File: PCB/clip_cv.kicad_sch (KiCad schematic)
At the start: 5 parts, among them J4 Input

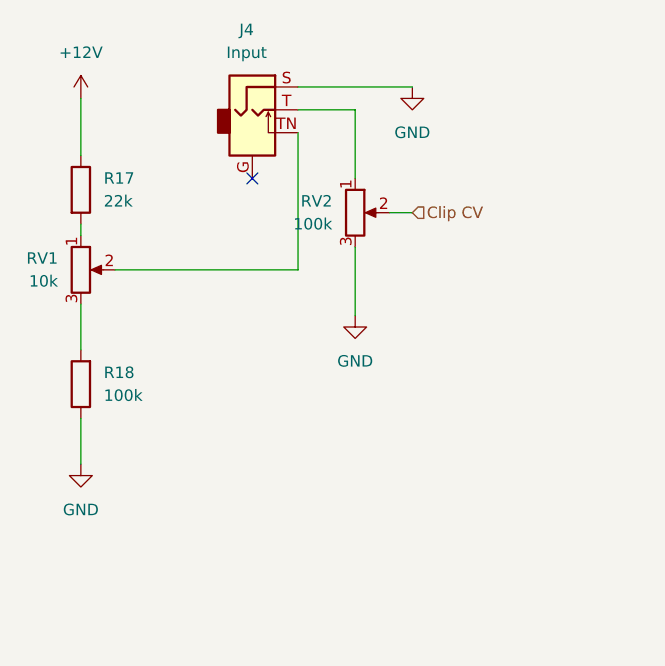
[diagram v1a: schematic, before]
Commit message: :art: Adjust layout of Clip CV input
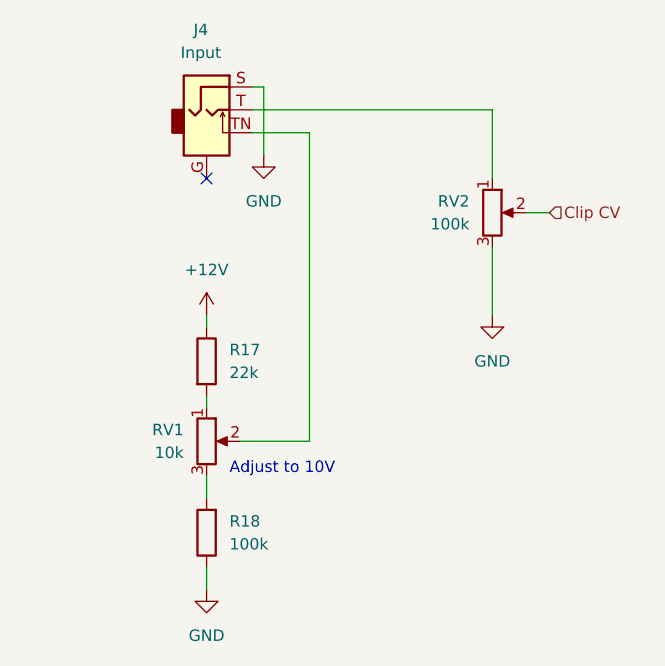
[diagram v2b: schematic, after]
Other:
- note added: "Adjust to 10V"
- moved on the sheet: J4, R17, R18, RV1, RV2

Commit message: :wrench: Re-assign component designators
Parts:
- renumbered R17 to R15, R18 to R16
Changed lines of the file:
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@@
   (symbol (lib_id "power:+12V") (at 149.86 102.87 0) (unit 1)
     (in_bom yes) (on_board yes) (dnp no) (fields_autoplaced)
-    (property "Reference" "#PWR0126" (at 149.86 106.68 0)
+    (property "Reference" "#PWR023" (at 149.86 106.68 0)
       (effects (font (size 1.27 1.27)) hide)
     )
@@
       (project "misterclippy"
         (path "/e63e39d7-6ac0-4ffd-8aa3-1841a4541b55/82b4cd66-2d39-4c64-8856-8f0d15c030b3"
-          (reference "#PWR0126") (unit 1)
-        )
-        (path "/e63e39d7-6ac0-4ffd-8aa3-1841a4541b55/99ffd22e-688e-45fd-ad48-7239527f44b1"
-          (reference "#PWR0130") (unit 1)
+          (reference "#PWR023") (unit 1)
+        )
+        (path "/e63e39d7-6ac0-4ffd-8aa3-1841a4541b55/99ffd22e-688e-45fd-ad48-7239527f44b1"
+          (reference "#PWR027") (unit 1)
         )
       )
@@
   (symbol (lib_id "Device:R") (at 149.86 107.95 0) (unit 1)
     (in_bom yes) (on_board yes) (dnp no) (fields_autoplaced)
-    (property "Reference" "R17" (at 152.4 106.6799 0)
+    (property "Reference" "R15" (at 152.4 106.6799 0)
       (effects (font (size 1.27 1.27)) (justify left))
     )
@@
       (project "misterclippy"
         (path "/e63e39d7-6ac0-4ffd-8aa3-1841a4541b55/82b4cd66-2d39-4c64-8856-8f0d15c030b3"
+          (reference "R15") (unit 1)
+        )
+        (path "/e63e39d7-6ac0-4ffd-8aa3-1841a4541b55/99ffd22e-688e-45fd-ad48-7239527f44b1"
           (reference "R17") (unit 1)
         )
-        (path "/e63e39d7-6ac0-4ffd-8aa3-1841a4541b55/99ffd22e-688e-45fd-ad48-7239527f44b1"
-          (reference "R19") (unit 1)
-        )
       )
     )
@@
   (symbol (lib_id "power:GND") (at 156.21 85.09 0) (unit 1)
     (in_bom yes) (on_board yes) (dnp no) (fields_autoplaced)
-    (property "Reference" "#PWR0127" (at 156.21 91.44 0)
+    (property "Reference" "#PWR025" (at 156.21 91.44 0)
       (effects (font (size 1.27 1.27)) hide)
     )
@@
       (project "misterclippy"
         (path "/e63e39d7-6ac0-4ffd-8aa3-1841a4541b55/82b4cd66-2d39-4c64-8856-8f0d15c030b3"
-          (reference "#PWR0127") (unit 1)
-        )
-        (path "/e63e39d7-6ac0-4ffd-8aa3-1841a4541b55/99ffd22e-688e-45fd-ad48-7239527f44b1"
-          (reference "#PWR0131") (unit 1)
+          (reference "#PWR025") (unit 1)
+        )
+        (path "/e63e39d7-6ac0-4ffd-8aa3-1841a4541b55/99ffd22e-688e-45fd-ad48-7239527f44b1"
+          (reference "#PWR029") (unit 1)
         )
       )
@@
   (symbol (lib_id "power:GND") (at 149.86 133.35 0) (unit 1)
     (in_bom yes) (on_board yes) (dnp no) (fields_autoplaced)
-    (property "Reference" "#PWR0125" (at 149.86 139.7 0)
+    (property "Reference" "#PWR024" (at 149.86 139.7 0)
       (effects (font (size 1.27 1.27)) hide)
     )
@@
       (project "misterclippy"
         (path "/e63e39d7-6ac0-4ffd-8aa3-1841a4541b55/82b4cd66-2d39-4c64-8856-8f0d15c030b3"
-          (reference "#PWR0125") (unit 1)
-        )
-        (path "/e63e39d7-6ac0-4ffd-8aa3-1841a4541b55/99ffd22e-688e-45fd-ad48-7239527f44b1"
-          (reference "#PWR0129") (unit 1)
+          (reference "#PWR024") (unit 1)
+        )
+        (path "/e63e39d7-6ac0-4ffd-8aa3-1841a4541b55/99ffd22e-688e-45fd-ad48-7239527f44b1"
+          (reference "#PWR028") (unit 1)
         )
       )
@@
   (symbol (lib_id "Device:R") (at 149.86 127 180) (unit 1)
     (in_bom yes) (on_board yes) (dnp no) (fields_autoplaced)
-    (property "Reference" "R18" (at 152.4 125.7299 0)
+    (property "Reference" "R16" (at 152.4 125.7299 0)
       (effects (font (size 1.27 1.27)) (justify right))
     )
@@
       (project "misterclippy"
         (path "/e63e39d7-6ac0-4ffd-8aa3-1841a4541b55/82b4cd66-2d39-4c64-8856-8f0d15c030b3"
+          (reference "R16") (unit 1)
+        )
+        (path "/e63e39d7-6ac0-4ffd-8aa3-1841a4541b55/99ffd22e-688e-45fd-ad48-7239527f44b1"
           (reference "R18") (unit 1)
         )
-        (path "/e63e39d7-6ac0-4ffd-8aa3-1841a4541b55/99ffd22e-688e-45fd-ad48-7239527f44b1"
-          (reference "R20") (unit 1)
-        )
       )
     )
@@
   (symbol (lib_id "power:GND") (at 181.61 102.87 0) (unit 1)
     (in_bom yes) (on_board yes) (dnp no) (fields_autoplaced)
-    (property "Reference" "#PWR0128" (at 181.61 109.22 0)
+    (property "Reference" "#PWR026" (at 181.61 109.22 0)
       (effects (font (size 1.27 1.27)) hide)
     )
@@
       (project "misterclippy"
         (path "/e63e39d7-6ac0-4ffd-8aa3-1841a4541b55/82b4cd66-2d39-4c64-8856-8f0d15c030b3"
-          (reference "#PWR0128") (unit 1)
-        )
-        (path "/e63e39d7-6ac0-4ffd-8aa3-1841a4541b55/99ffd22e-688e-45fd-ad48-7239527f44b1"
-          (reference "#PWR0132") (unit 1)
-        )
-      )
+          (reference "#PWR026") (unit 1)
+        )
+        (path "/e63e39d7-6ac0-4ffd-8aa3-1841a4541b55/99ffd22e-688e-45fd-ad48-7239527f44b1"
+          (reference "#PWR030") (unit 1)
+        )
+      )

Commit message: :wrench: Replace audio jack footprints by centered versions
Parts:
- J4: footprint Connector_Audio:Jack_3.5mm_QingPu_WQP-PJ398SM_Vertical_CircularHoles -> mopsy:Jack_3.5mm_QingPu_WQP-PJ398SM_Vertical_CircularHoles_Centered
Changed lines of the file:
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@@
       (effects (font (size 1.27 1.27)))
     )
-    (property "Footprint" "Connector_Audio:Jack_3.5mm_QingPu_WQP-PJ398SM_Vertical_CircularHoles" (at 149.86 80.01 0)
+    (property "Footprint" "mopsy:Jack_3.5mm_QingPu_WQP-PJ398SM_Vertical_CircularHoles_Centered" (at 149.86 80.01 0)
       (effects (font (size 1.27 1.27)) hide)
     )

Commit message: :art: Turn poti direction around
Make sure that turning the poti clockwise increases the setting.
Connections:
- net GND: now also RV2.1; no longer RV2.3
- net at R15.2: now also RV1.3; no longer RV1.1
- net at R16.2: now also RV1.1; no longer RV1.3
- net at J4.T: now also RV2.3; no longer RV2.1
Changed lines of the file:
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@@
     )
   )
-  (symbol (lib_id "Device:R_Potentiometer") (at 149.86 116.84 0) (unit 1)
-    (in_bom yes) (on_board yes) (dnp no) (fields_autoplaced)
-    (property "Reference" "RV1" (at 147.32 115.5699 0)
+  (symbol (lib_id "Device:R_Potentiometer") (at 149.86 116.84 0) (mirror x) (unit 1)
+    (in_bom yes) (on_board yes) (dnp no)
+    (property "Reference" "RV1" (at 147.32 118.1101 0)
       (effects (font (size 1.27 1.27)) (justify right))
     )
-    (property "Value" "10k" (at 147.32 118.1099 0)
+    (property "Value" "10k" (at 147.32 115.5701 0)
       (effects (font (size 1.27 1.27)) (justify right))
     )
@@
     )
   )
-  (symbol (lib_id "Device:R_Potentiometer") (at 181.61 91.44 0) (unit 1)
-    (in_bom yes) (on_board yes) (dnp no) (fields_autoplaced)
-    (property "Reference" "RV2" (at 179.07 90.1699 0)
+  (symbol (lib_id "Device:R_Potentiometer") (at 181.61 91.44 0) (mirror x) (unit 1)
+    (in_bom yes) (on_board yes) (dnp no)
+    (property "Reference" "RV2" (at 179.07 92.7101 0)
       (effects (font (size 1.27 1.27)) (justify right))
     )
-    (property "Value" "100k" (at 179.07 92.7099 0)
+    (property "Value" "100k" (at 179.07 90.1701 0)
       (effects (font (size 1.27 1.27)) (justify right))
     )

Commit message: :art: Apply geographical reannotation
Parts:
- renumbered J4 to J5, R16 to R15, R15 to R16, RV2 to RV1, RV1 to RV4
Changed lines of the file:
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@@
   (symbol (lib_id "Device:R") (at 149.86 107.95 0) (unit 1)
     (in_bom yes) (on_board yes) (dnp no) (fields_autoplaced)
-    (property "Reference" "R15" (at 152.4 106.6799 0)
+    (property "Reference" "R16" (at 152.4 106.6799 0)
       (effects (font (size 1.27 1.27)) (justify left))
     )
@@
       (project "misterclippy"
         (path "/e63e39d7-6ac0-4ffd-8aa3-1841a4541b55/82b4cd66-2d39-4c64-8856-8f0d15c030b3"
-          (reference "R15") (unit 1)
+          (reference "R16") (unit 1)
         )
         (path "/e63e39d7-6ac0-4ffd-8aa3-1841a4541b55/99ffd22e-688e-45fd-ad48-7239527f44b1"
-          (reference "R17") (unit 1)
+          (reference "R14") (unit 1)
         )
       )
@@
   (symbol (lib_id "Device:R_Potentiometer") (at 149.86 116.84 0) (mirror x) (unit 1)
     (in_bom yes) (on_board yes) (dnp no)
-    (property "Reference" "RV1" (at 147.32 118.1101 0)
+    (property "Reference" "RV4" (at 147.32 118.1101 0)
       (effects (font (size 1.27 1.27)) (justify right))
     )
@@
       (project "misterclippy"
         (path "/e63e39d7-6ac0-4ffd-8aa3-1841a4541b55/82b4cd66-2d39-4c64-8856-8f0d15c030b3"
-          (reference "RV1") (unit 1)
+          (reference "RV4") (unit 1)
         )
         (path "/e63e39d7-6ac0-4ffd-8aa3-1841a4541b55/99ffd22e-688e-45fd-ad48-7239527f44b1"
@@
   (symbol (lib_id "Device:R_Potentiometer") (at 181.61 91.44 0) (mirror x) (unit 1)
     (in_bom yes) (on_board yes) (dnp no)
-    (property "Reference" "RV2" (at 179.07 92.7101 0)
+    (property "Reference" "RV1" (at 179.07 92.7101 0)
       (effects (font (size 1.27 1.27)) (justify right))
     )
@@
       (project "misterclippy"
         (path "/e63e39d7-6ac0-4ffd-8aa3-1841a4541b55/82b4cd66-2d39-4c64-8856-8f0d15c030b3"
-          (reference "RV2") (unit 1)
+          (reference "RV1") (unit 1)
         )
         (path "/e63e39d7-6ac0-4ffd-8aa3-1841a4541b55/99ffd22e-688e-45fd-ad48-7239527f44b1"
-          (reference "RV4") (unit 1)
+          (reference "RV2") (unit 1)
         )
       )
@@
   (symbol (lib_id "Connector:AudioJack2_Ground_SwitchT") (at 149.86 80.01 0) (unit 1)
     (in_bom yes) (on_board yes) (dnp no) (fields_autoplaced)
-    (property "Reference" "J4" (at 149.225 71.12 0)
+    (property "Reference" "J5" (at 149.225 71.12 0)
       (effects (font (size 1.27 1.27)))
     )
@@
       (project "misterclippy"
         (path "/e63e39d7-6ac0-4ffd-8aa3-1841a4541b55/82b4cd66-2d39-4c64-8856-8f0d15c030b3"
-          (reference "J4") (unit 1)
+          (reference "J5") (unit 1)
         )
         (path "/e63e39d7-6ac0-4ffd-8aa3-1841a4541b55/99ffd22e-688e-45fd-ad48-7239527f44b1"
-          (reference "J5") (unit 1)
+          (reference "J6") (unit 1)
         )
       )
@@
   (symbol (lib_id "Device:R") (at 149.86 127 180) (unit 1)
     (in_bom yes) (on_board yes) (dnp no) (fields_autoplaced)
-    (property "Reference" "R16" (at 152.4 125.7299 0)
+    (property "Reference" "R15" (at 152.4 125.7299 0)
       (effects (font (size 1.27 1.27)) (justify right))
     )
@@
       (project "misterclippy"
         (path "/e63e39d7-6ac0-4ffd-8aa3-1841a4541b55/82b4cd66-2d39-4c64-8856-8f0d15c030b3"
-          (reference "R16") (unit 1)
+          (reference "R15") (unit 1)
         )
         (path "/e63e39d7-6ac0-4ffd-8aa3-1841a4541b55/99ffd22e-688e-45fd-ad48-7239527f44b1"
-          (reference "R18") (unit 1)
+          (reference "R13") (unit 1)
         )
       )

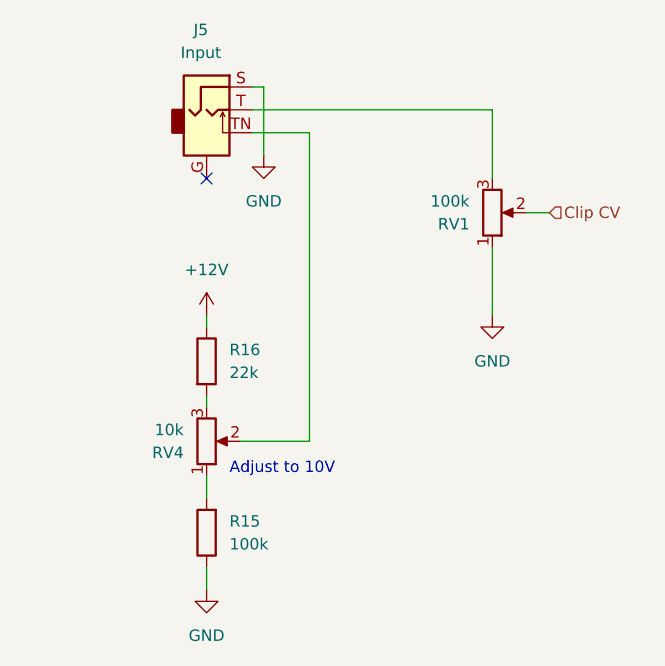
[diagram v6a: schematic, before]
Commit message: :art: Adjust voltage divider for Clip CV tap
Adjust the voltage divider so that 10V are within a good
adjustment range.
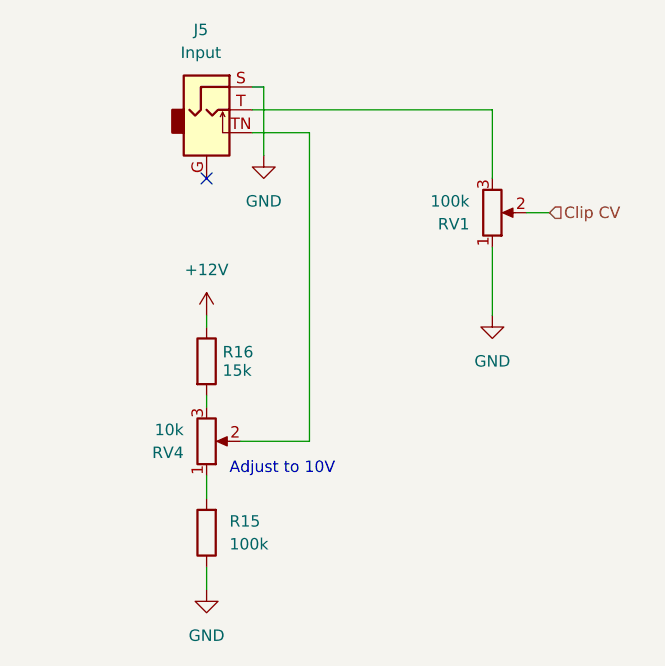
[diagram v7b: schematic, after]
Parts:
- R16: value 22k -> 15k
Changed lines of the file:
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@@
   (symbol (lib_id "Device:R") (at 149.86 107.95 0) (unit 1)
     (in_bom yes) (on_board yes) (dnp no) (fields_autoplaced)
-    (property "Reference" "R16" (at 152.4 106.6799 0)
+    (property "Reference" "R16" (at 151.638 106.926 0)
       (effects (font (size 1.27 1.27)) (justify left))
     )
-    (property "Value" "22k" (at 152.4 109.2199 0)
+    (property "Value" "15k" (at 151.638 108.974 0)
       (effects (font (size 1.27 1.27)) (justify left))
     )

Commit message: :wrench: Adjust the voltage dividers for Clip CV
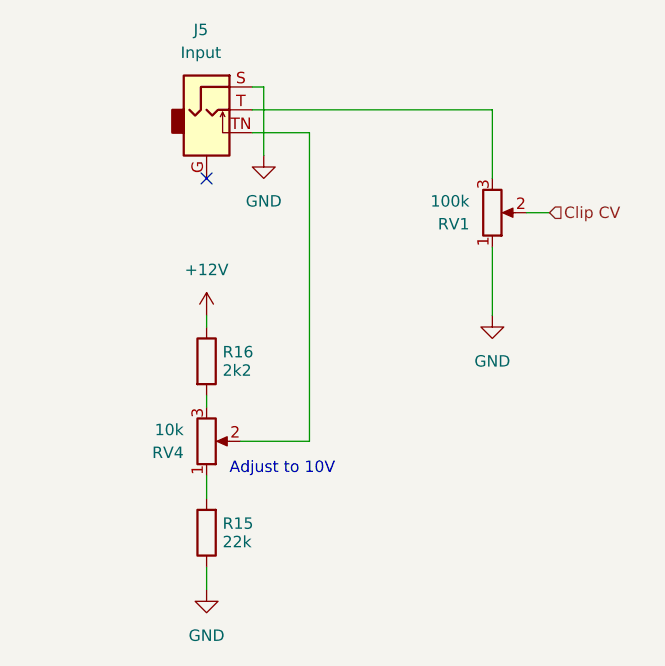
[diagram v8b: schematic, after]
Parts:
- R15: value 100k -> 22k
- R16: value 15k -> 2k2
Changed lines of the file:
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@@
       (effects (font (size 1.27 1.27)) (justify left))
     )
-    (property "Value" "15k" (at 151.638 108.974 0)
+    (property "Value" "2k2" (at 151.638 108.974 0)
       (effects (font (size 1.27 1.27)) (justify left))
     )
@@
   (symbol (lib_id "Device:R") (at 149.86 127 180) (unit 1)
     (in_bom yes) (on_board yes) (dnp no) (fields_autoplaced)
-    (property "Reference" "R15" (at 152.4 125.7299 0)
+    (property "Reference" "R15" (at 151.638 125.976 0)
       (effects (font (size 1.27 1.27)) (justify right))
     )
-    (property "Value" "100k" (at 152.4 128.2699 0)
+    (property "Value" "22k" (at 151.638 128.024 0)
       (effects (font (size 1.27 1.27)) (justify right))
     )
